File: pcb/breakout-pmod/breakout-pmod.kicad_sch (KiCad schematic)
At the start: 13 parts, among them J1 FX18-120P-0.8SV20

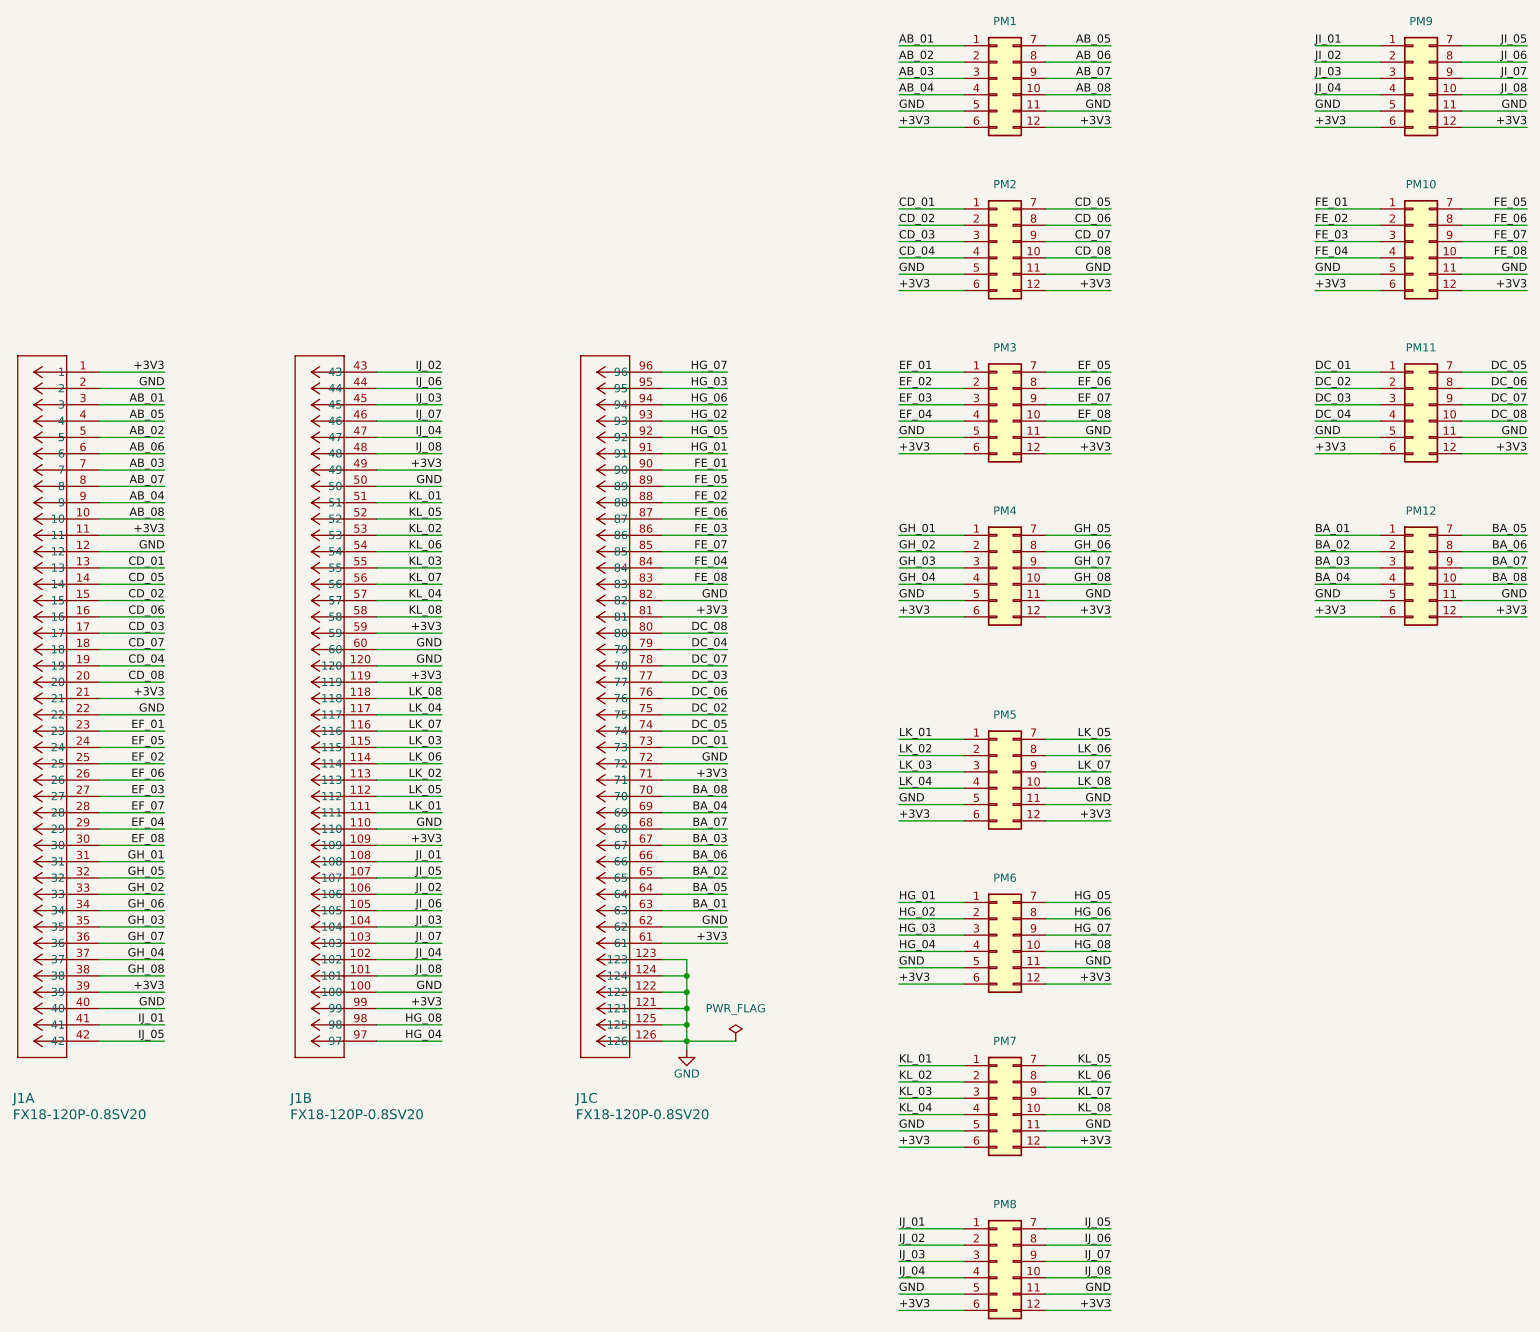
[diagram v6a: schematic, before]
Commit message: [pcb][pmod] switch to single letter labels
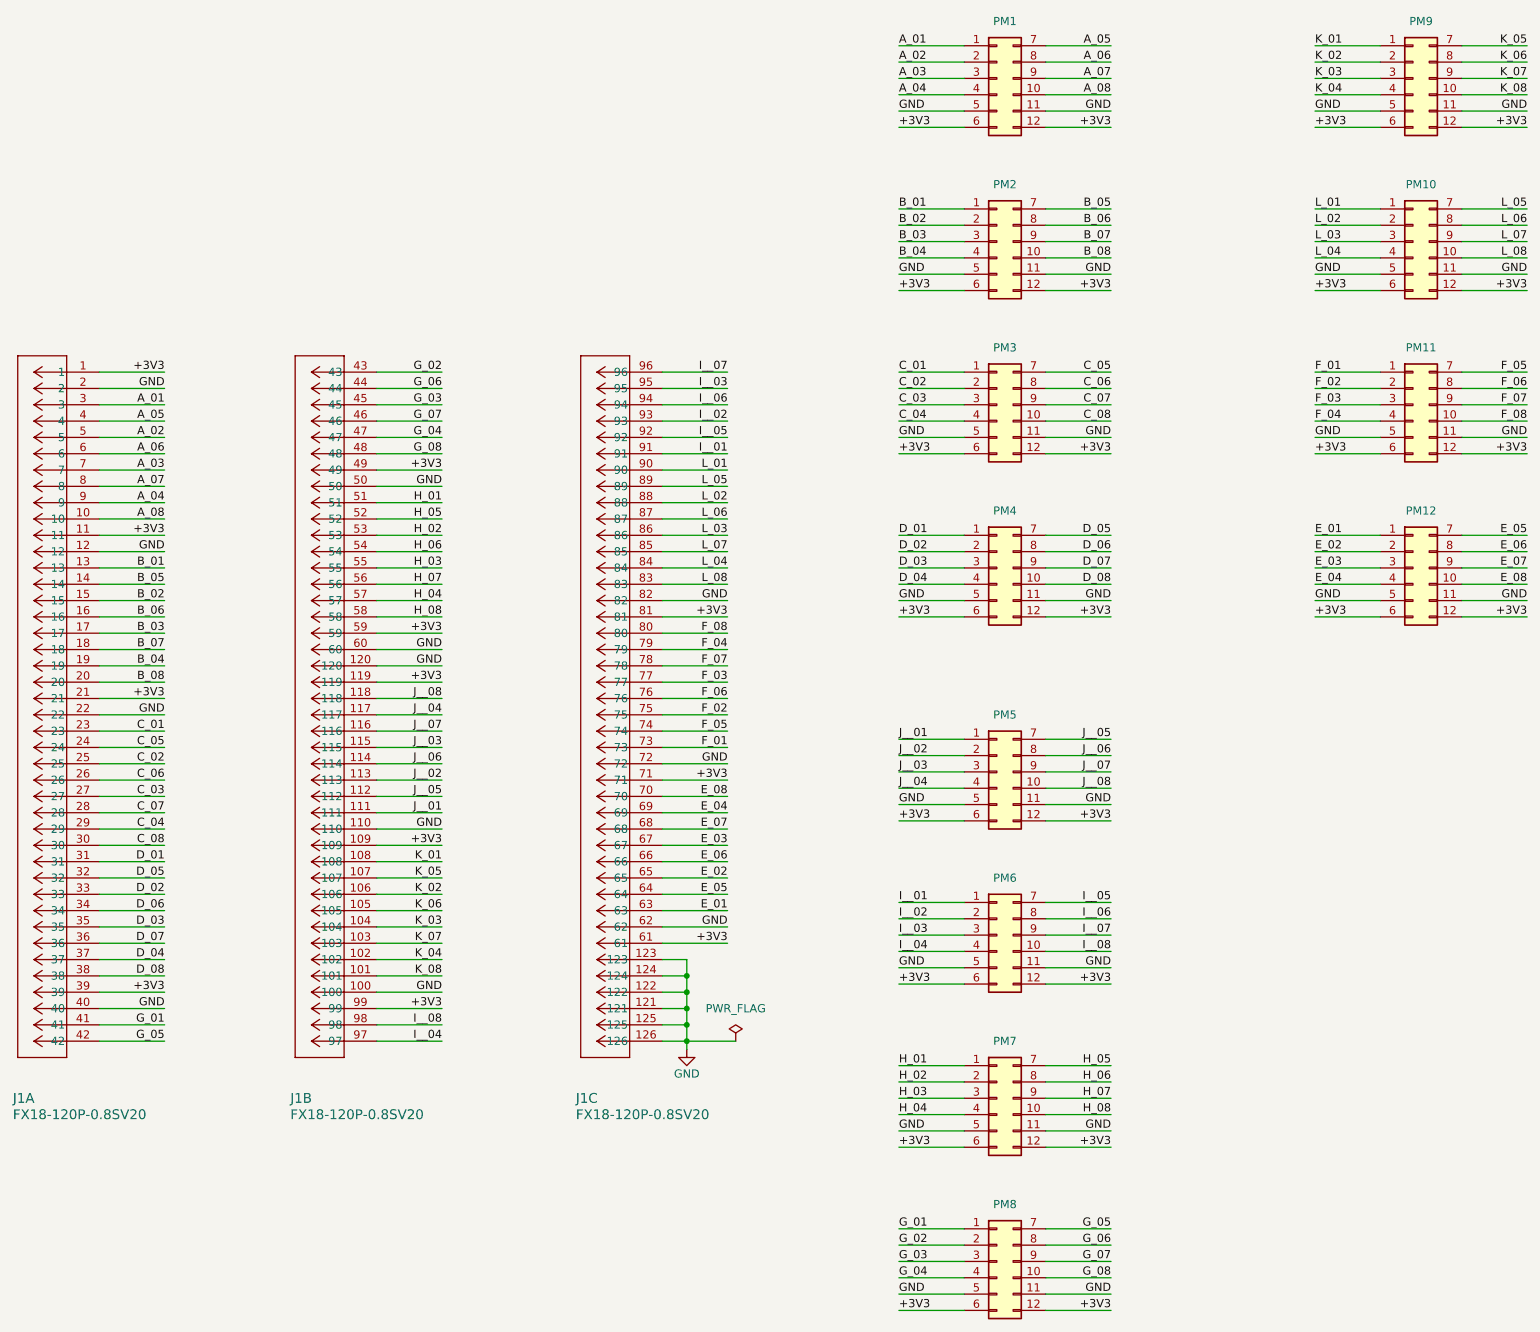
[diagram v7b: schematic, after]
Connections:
- net AB_01 renamed A_01
- net AB_02 renamed A_02
- net AB_03 renamed A_03
- net AB_04 renamed A_04
- net AB_05 renamed A_05
- net AB_06 renamed A_06
- net AB_07 renamed A_07
- net AB_08 renamed A_08
- net BA_01 renamed E_01
- net BA_02 renamed E_02
- net BA_03 renamed E_03
- net BA_04 renamed E_04
- net BA_05 renamed E_05
- net BA_06 renamed E_06
- net BA_07 renamed E_07
- net BA_08 renamed E_08
- net CD_01 renamed B_01
- net CD_02 renamed B_02
- net CD_03 renamed B_03
- net CD_04 renamed B_04
- net CD_05 renamed B_05
- net CD_06 renamed B_06
- net CD_07 renamed B_07
- net CD_08 renamed B_08
- net DC_01 renamed F_01
- net DC_02 renamed F_02
- net DC_03 renamed F_03
- net DC_04 renamed F_04
- net DC_05 renamed F_05
- net DC_06 renamed F_06
- net DC_07 renamed F_07
- net DC_08 renamed F_08
- net EF_01 renamed C_01
- net EF_02 renamed C_02
- net EF_03 renamed C_03
- net EF_04 renamed C_04
- net EF_05 renamed C_05
- net EF_06 renamed C_06
- net EF_07 renamed C_07
- net EF_08 renamed C_08
- net FE_01 renamed L_01
- net FE_02 renamed L_02
- net FE_03 renamed L_03
- net FE_04 renamed L_04
- net FE_05 renamed L_05
- net FE_06 renamed L_06
- net FE_07 renamed L_07
- net FE_08 renamed L_08
- net GH_01 renamed D_01
- net GH_02 renamed D_02
- net GH_03 renamed D_03
- net GH_04 renamed D_04
- net GH_05 renamed D_05
- net GH_06 renamed D_06
- net GH_07 renamed D_07
- net GH_08 renamed D_08
- net HG_01 renamed I__01
- net HG_02 renamed I__02
- net HG_03 renamed I__03
- net HG_04 renamed I__04
- net HG_05 renamed I__05
- net HG_06 renamed I__06
- net HG_07 renamed I__07
- net HG_08 renamed I__08
- net IJ_01 renamed G_01
- net IJ_02 renamed G_02
- net IJ_03 renamed G_03
- net IJ_04 renamed G_04
- net IJ_05 renamed G_05
- net IJ_06 renamed G_06
- net IJ_07 renamed G_07
- net IJ_08 renamed G_08
- net JI_01 renamed K_01
- net JI_02 renamed K_02
- net JI_03 renamed K_03
- net JI_04 renamed K_04
- net JI_05 renamed K_05
- net JI_06 renamed K_06
- net JI_07 renamed K_07
- net JI_08 renamed K_08
- net KL_01 renamed H_01
- net KL_02 renamed H_02
- net KL_03 renamed H_03
- net KL_04 renamed H_04
- net KL_05 renamed H_05
- net KL_06 renamed H_06
- net KL_07 renamed H_07
- net KL_08 renamed H_08
- net LK_01 renamed J__01
- net LK_02 renamed J__02
- net LK_03 renamed J__03
- net LK_04 renamed J__04
- net LK_05 renamed J__05
- net LK_06 renamed J__06
- net LK_07 renamed J__07
- net LK_08 renamed J__08

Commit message: [pcb]pmod] stitching vias
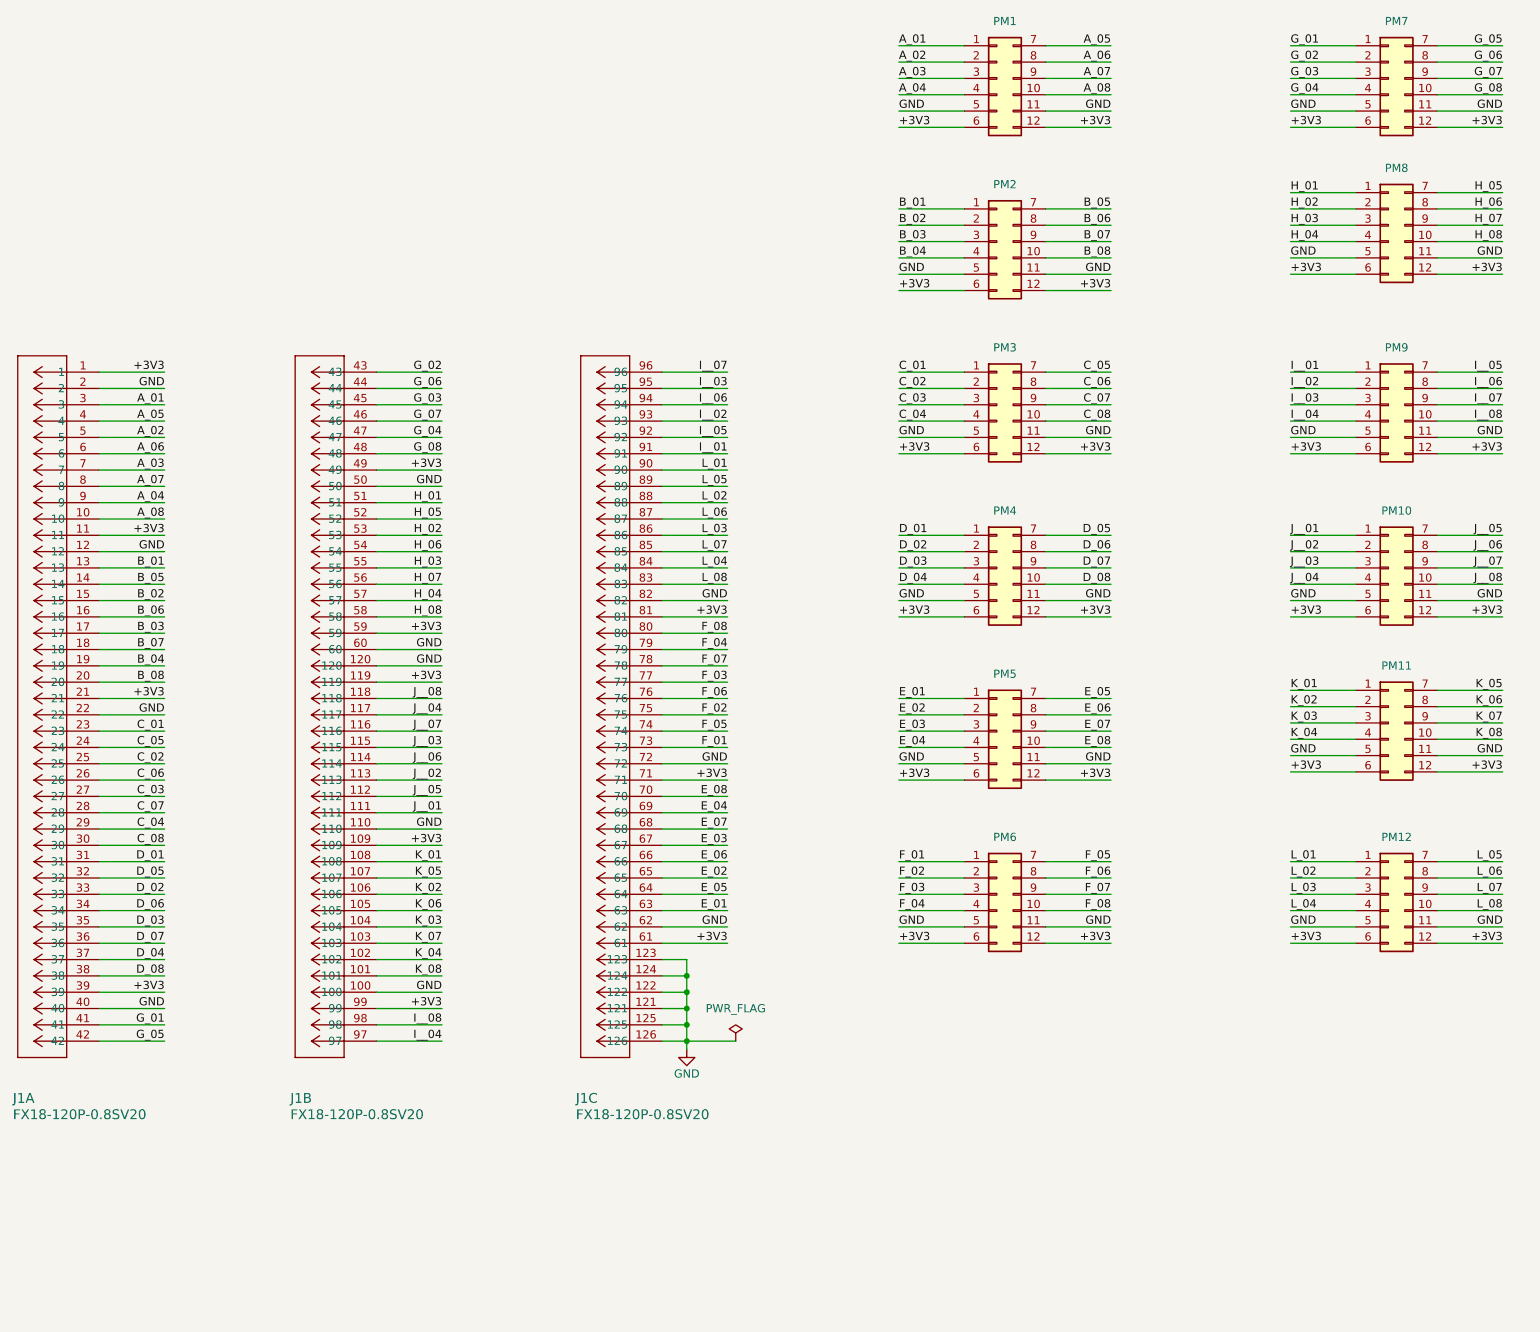
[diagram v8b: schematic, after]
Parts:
- renumbered PM5 to PM10, PM9 to PM11, PM10 to PM12, PM12 to PM5, PM11 to PM6, PM8 to PM7, PM7 to PM8, PM6 to PM9
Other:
- moved on the sheet: PM10, PM11, PM12, PM5, PM6, PM7, PM8, PM9
